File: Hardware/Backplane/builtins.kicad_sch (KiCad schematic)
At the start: 45 parts, among them J1001 Conn_01x06, J1002 Conn_01x06, J1003 Conn_01x06, J1004 Conn_01x06, Q1001 NMOS, Q1002 NMOS, Q1003 NMOS, SW1001 SW_Push, U1001 OSC48M-3.3I/S3-20T, U1003 CD74HC221M96, U1004 PCF8523T/1,118, Y1001 32.768k

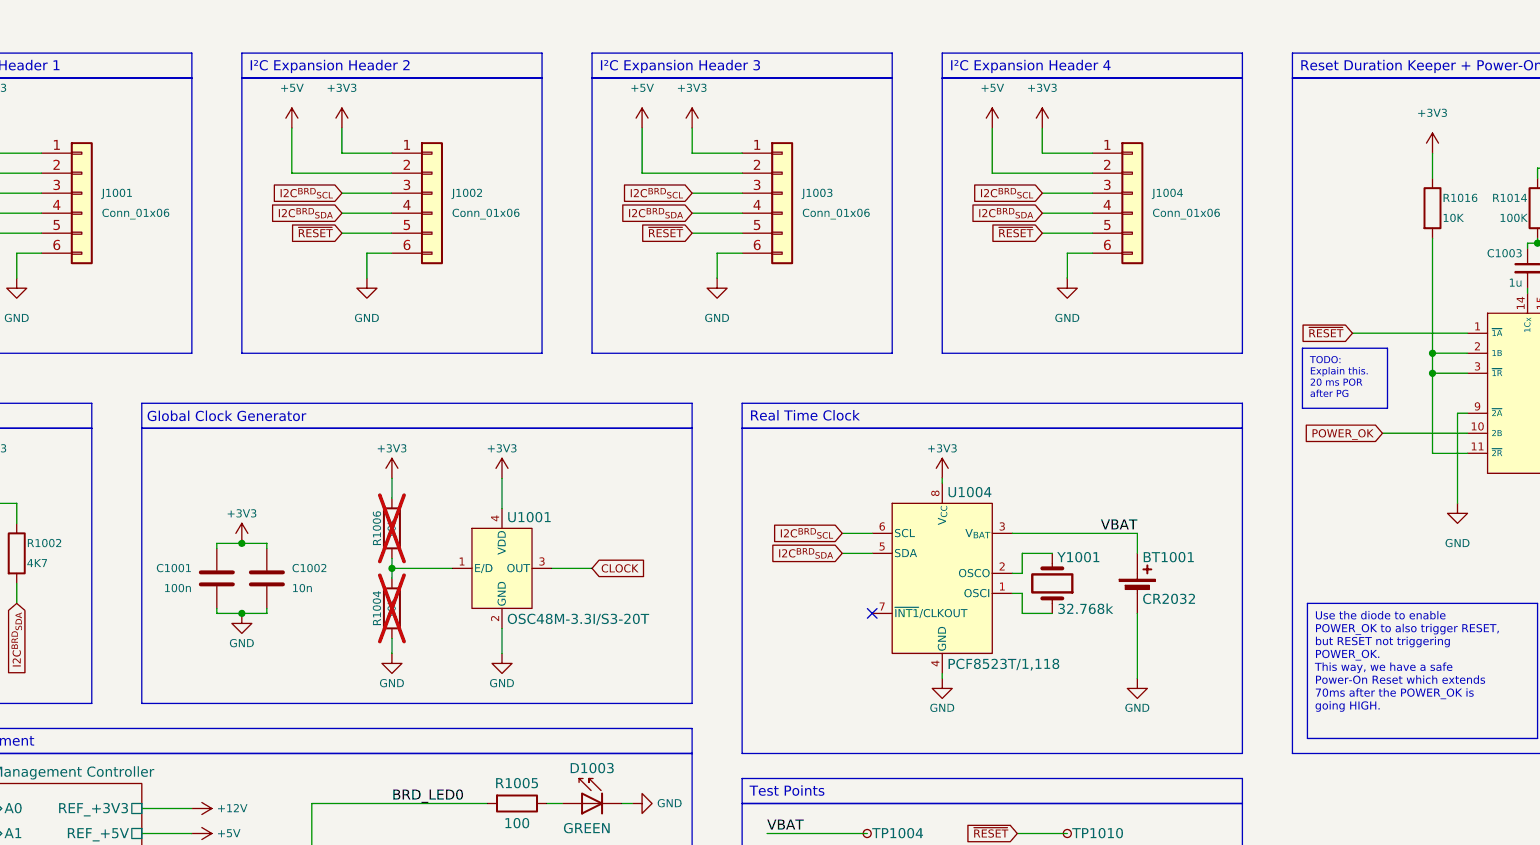
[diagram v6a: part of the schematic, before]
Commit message: Refactors clock system to use AND gates for clock tree spanning and gating.
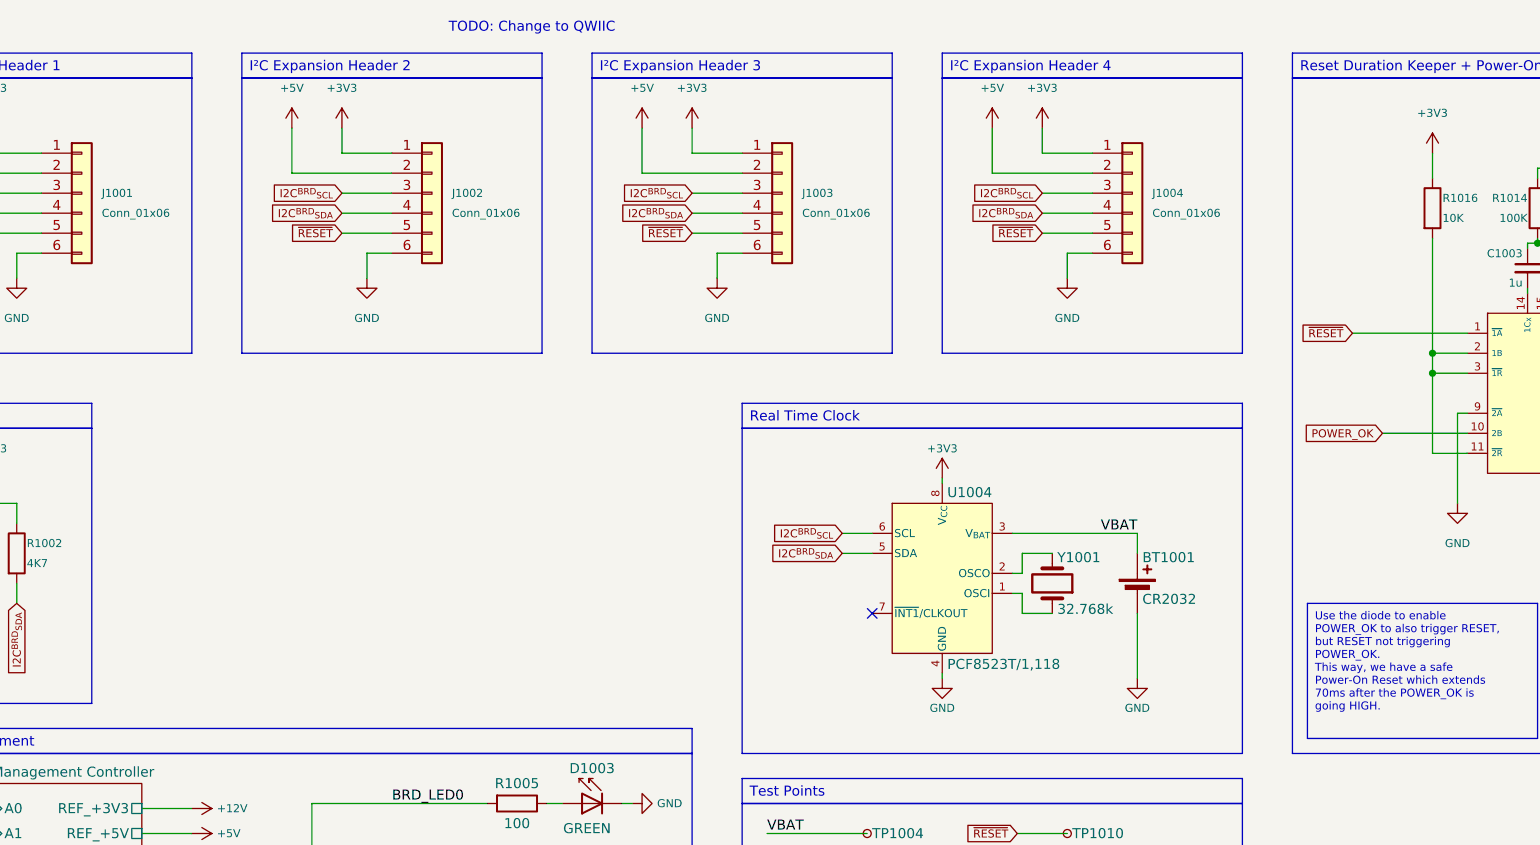
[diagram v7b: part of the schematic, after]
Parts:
- removed C1001: 100n, Capacitor_SMD:C_0603_1608Metric, symbol Device:C
- removed C1002: 10n, Capacitor_SMD:C_0603_1608Metric, symbol Device:C
- removed R1004, R1006: 10K, Resistor_SMD:R_0603_1608Metric, symbol Device:R
- removed U1001: OSC48M-3.3I/S3-20T, symbol Home Computer:OSC48M-3.3I/S3-20T
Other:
- note added: "TODO: Change to QWIIC"
- note removed: "Global Clock Generator"

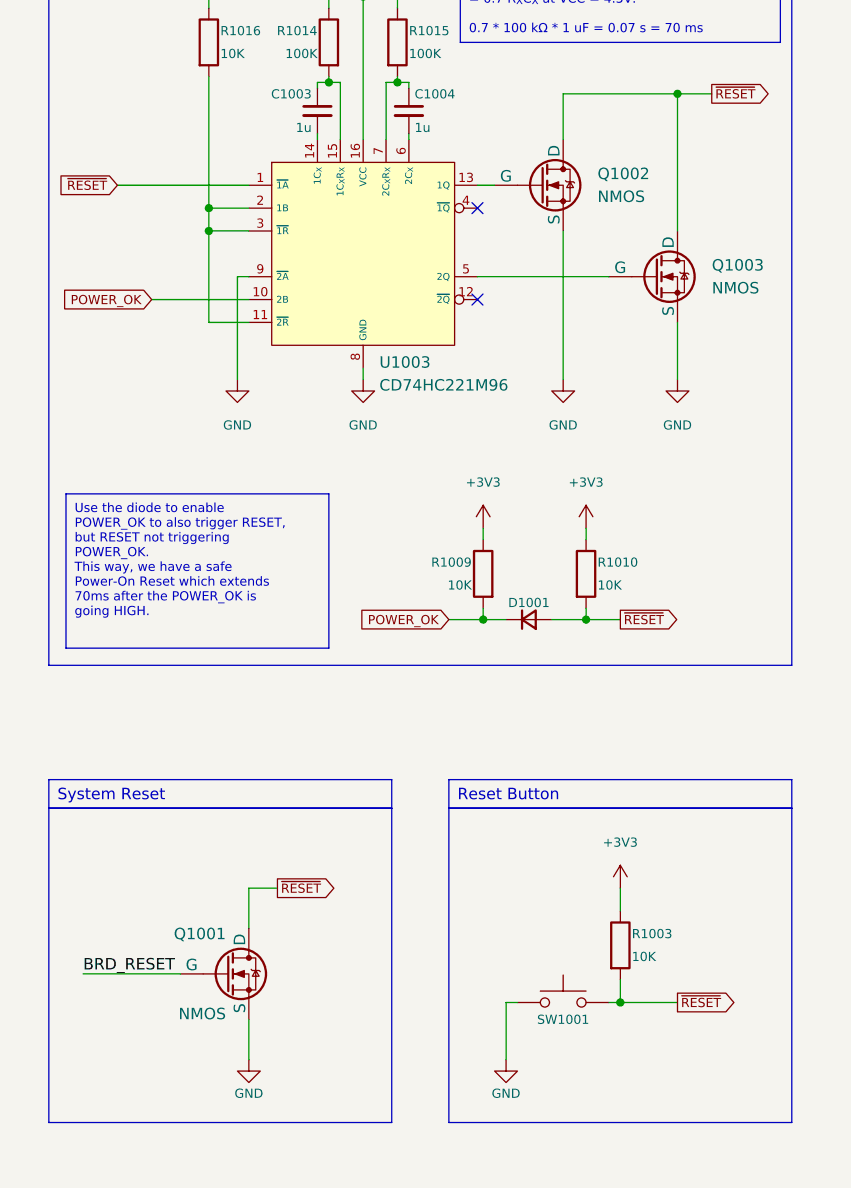
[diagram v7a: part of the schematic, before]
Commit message: Some cleanups of Backplane schematic: Adds DigiKey part numbers, removes unnecessary properties, marks test points as excluded from BOM
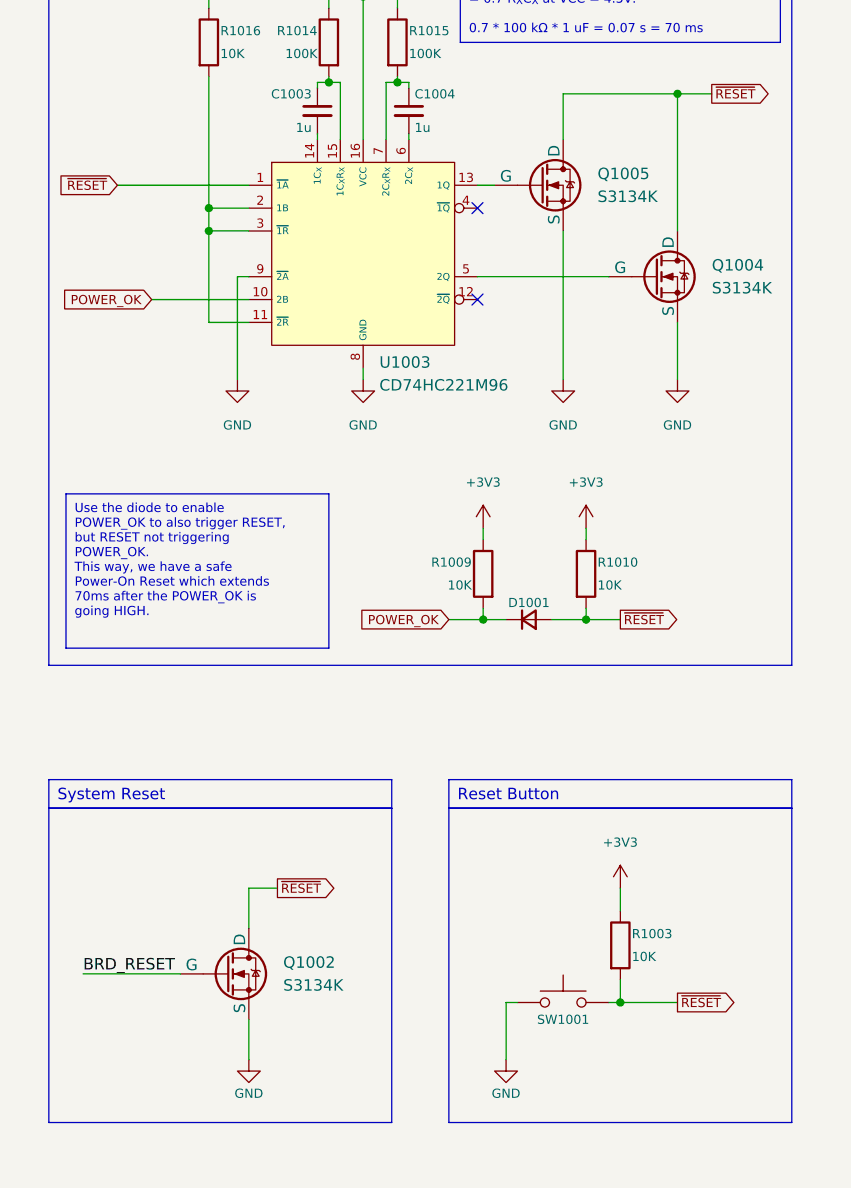
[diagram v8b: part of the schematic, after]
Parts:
- removed Q1001, Q1003: NMOS, Package_TO_SOT_SMD:SOT-23, symbol Simulation_SPICE:NMOS
- added Q1004, Q1005: S3134K, symbol Simulation_SPICE:NMOS
- Q1002: value NMOS -> S3134K; footprint Package_TO_SOT_SMD:SOT-23 -> (none); Digikey Part No (none) -> 4786-S3134KCT-ND
- TP1001, TP1002, TP1003, TP1004, TP1005, TP1006, TP1007, TP1008, TP1009, TP1010: now left out of the parts list
- U1003: Digikey Part No (none) -> 296-17789-1-ND
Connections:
- net BRD_RESET: now also Q1002.2 (G)
- net GND: now also Q1004.3 (S), Q1005.3 (S)
- net ~{RESET}: now also Q1004.1 (D), Q1005.1 (D)
- net at U1003.13 (1Q): now also Q1005.2 (G); no longer Q1002.2 (G)
- net at U1003.5 (2Q): now also Q1004.2 (G)
